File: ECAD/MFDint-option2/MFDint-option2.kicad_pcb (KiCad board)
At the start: 2 copper layers, 113 x 109 mm, 47 parts, among them J1 Conn_02x03_Odd_Even, J2 Conn_01x04, J3 Conn_01x04, J4 Conn_02x03_Odd_Even, J5 Conn_01x04, J6 Conn_01x04, SW11 SW_Push, SW12 SW_Push, SW13 SW_Push, SW14 SW_Push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

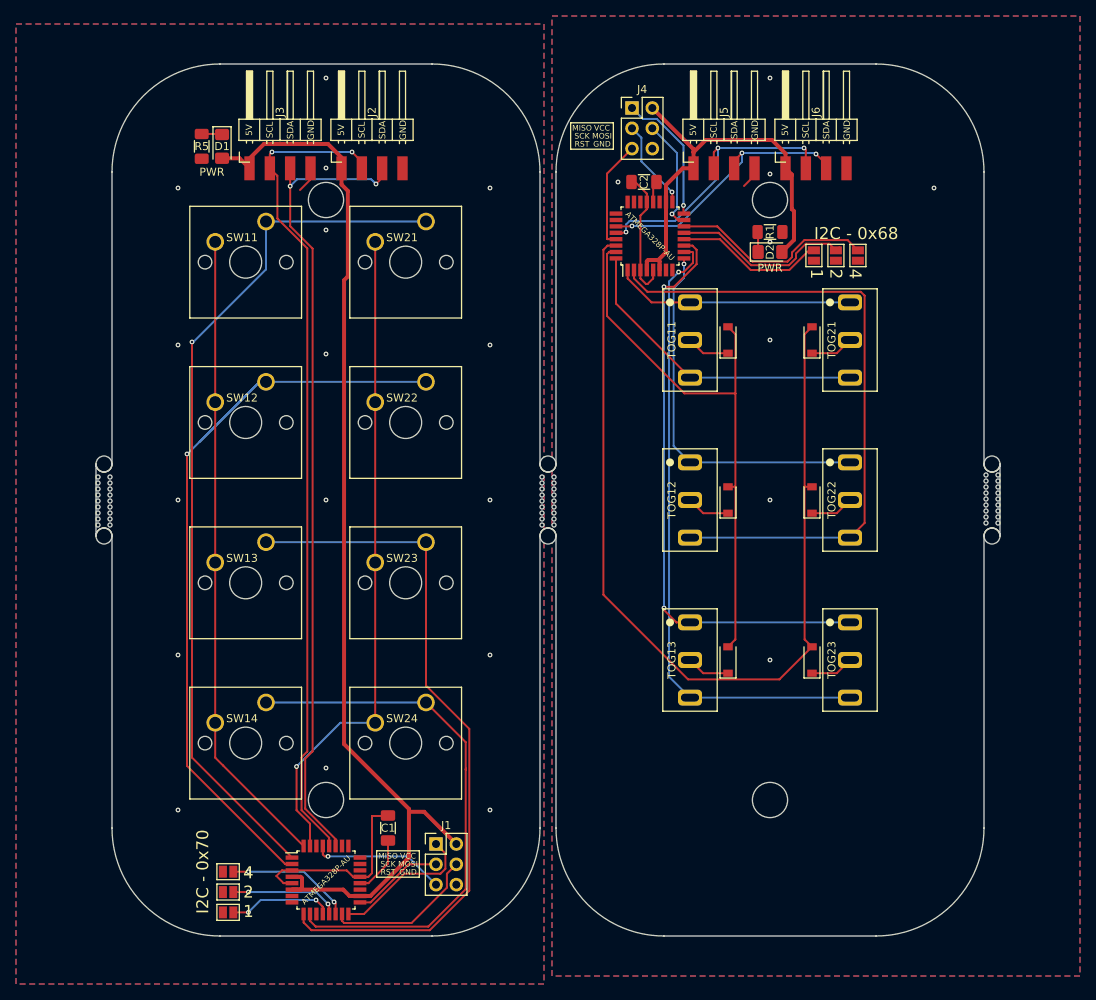
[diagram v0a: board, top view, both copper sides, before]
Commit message: Removing panelisations, adding polyfuses
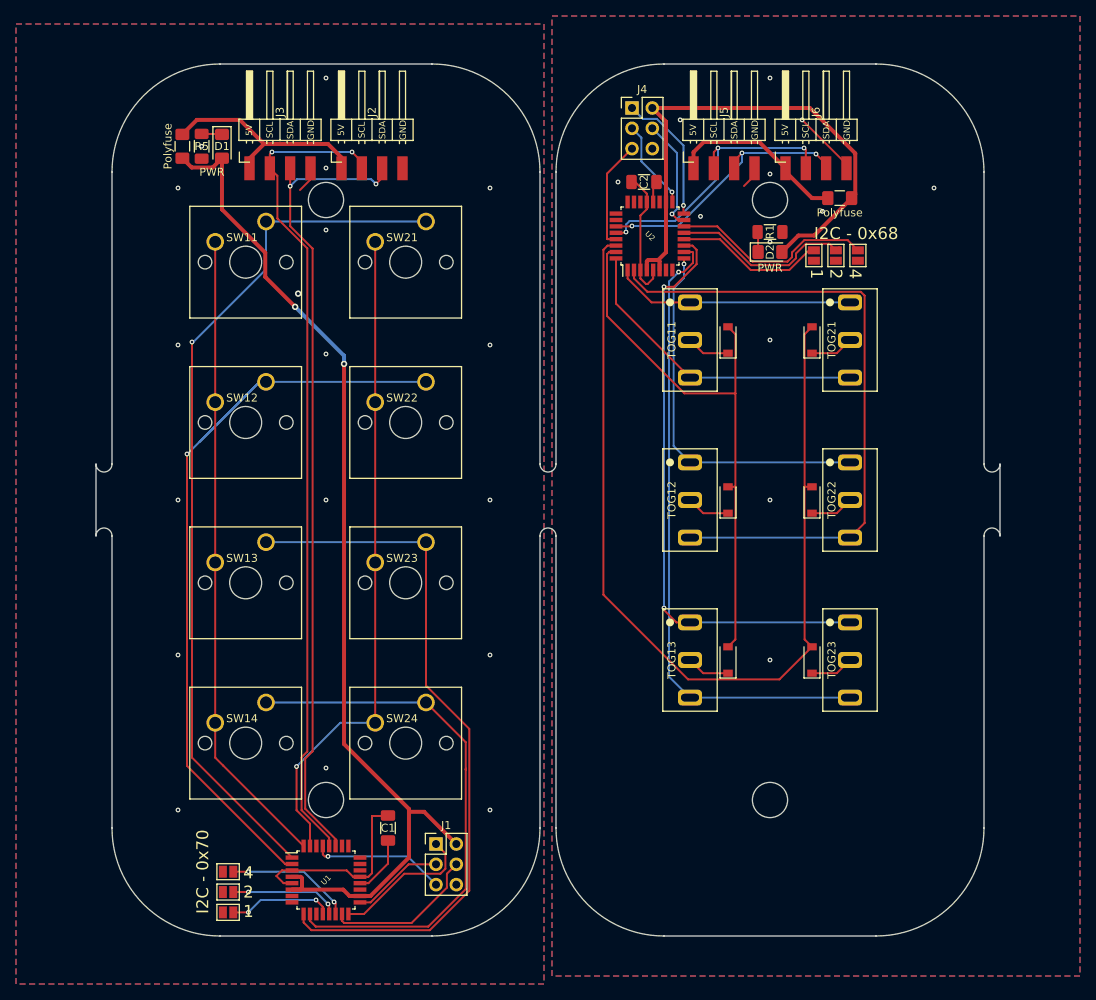
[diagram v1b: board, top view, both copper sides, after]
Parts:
- removed G*** (x2): LOGO, mycustomlibrary:CBB_1inch
- removed REF** (x2): ICSP-Silk, mycustomlibrary:ICSP-Silk
- removed mouse-bite-2mm-slot (x3): VAL**, Panelisation:mouse-bite-2mm-slot-5mm-width
- added Polyfuse: Polyfuse, Fuse:Fuse_1206_3216Metric_Pad1.42x1.75mm_HandSolder, F.Cu at (93.0, 16.8)
- added Polyfuse: Polyfuse, Fuse:Fuse_1206_3216Metric_Pad1.42x1.75mm_HandSolder, F.Cu at (10.8, 10.3)
- renumbered ATMEGA328P-AU to U1, ATMEGA328P-AU to U2
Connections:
- J2 pad 1: +5V -> Net-(F1-Pad2)
- J3 pad 1: +5V -> Net-(F1-Pad2)
- J5 pad 1: VCC -> Net-(F2-Pad2)
- J6 pad 1: VCC -> Net-(F2-Pad2)
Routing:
- net Net-(F1-Pad2): track 0.00 -> 28.6 mm
- net Net-(F2-Pad2): track 0.00 -> 22.5 mm
- net VCC: track 53.9 -> 69.0 mm
- net GNDREF: track 19.4 -> 27.8 mm, vias 8 -> 12
- net +5V: track 138.8 -> 131.4 mm, vias 0 -> 2
- net GND: vias 16 -> 18

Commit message: Change from 1x04 2.54mm headers to 1x05 micro JST
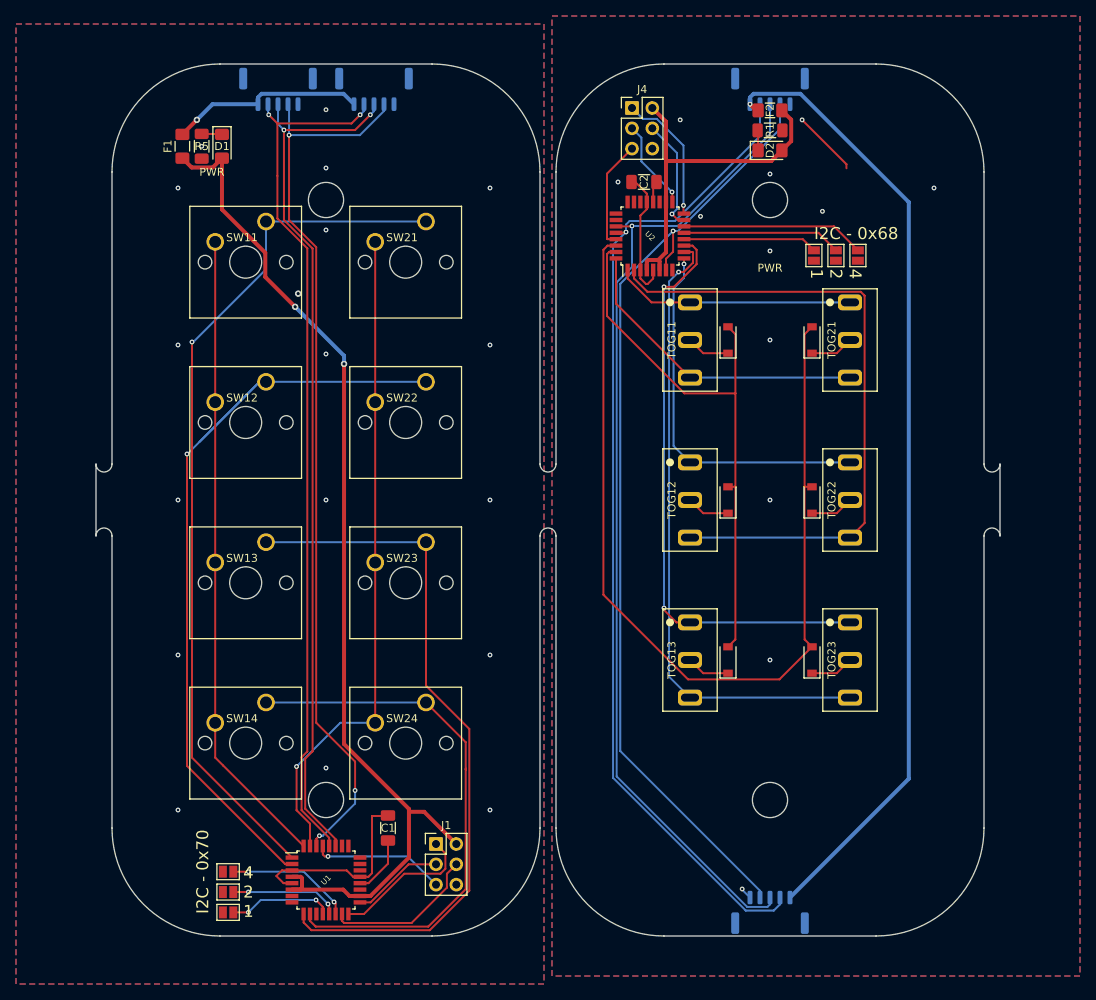
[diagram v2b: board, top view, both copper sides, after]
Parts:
- J2, J3, J5, J6: value Conn_01x04 -> Conn_01x05; footprint mycustomlibrary:PinHeader_1x04_P2.54mm_Horizontal_SMD -> Connector_JST:JST_GH_SM05B-GHS-TB_1x05-1MP_P1.25mm_Horizontal; moved to B.Cu
- moved J5 95.2 mm to (84.2, 106.0), turned to 180 degrees
- moved J2 14.1 mm to (22.8, 3.17), turned to 0 degrees
- moved J3 14.1 mm to (34.8, 3.17), turned to 0 degrees
- moved F2 14.0 mm to (84.2, 5.80)
- moved D2 12.7 mm to (84.2, 10.8)
- moved R1 12.7 mm to (84.2, 8.30)
- moved J6 9.71 mm to (84.2, 3.17), turned to 0 degrees
- renumbered Polyfuse to F1, Polyfuse to F2
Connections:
- J2 pad 4: GND -> /BUS_SIGNAL
- J3 pad 4: GND -> /BUS_SIGNAL
- J5 pad 4: GNDREF -> /BUS_SIGNAL2
- J6 pad 4: GNDREF -> /BUS_SIGNAL2
- U1 pad 30: Net-(U1-Pad30) -> /BUS_SIGNAL
- U2 pad 7: Net-(U2-Pad7) -> /BUS_SIGNAL2
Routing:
- net /BUS_SIGNAL2: track 0.00 -> 120.3 mm, vias 0 -> 1
- net /BUS_SIGNAL: track 0.00 -> 112.4 mm, vias 0 -> 3
- net Net-(F2-Pad2): track 22.5 -> 120.9 mm, vias 0 -> 1
- net SDA2: track 34.1 -> 124.3 mm, vias 3 -> 1
- net SCL2: track 36.0 -> 125.3 mm, vias 3 -> 1
- net VCC: track 69.0 -> 45.1 mm
- net SDA: track 101.5 -> 110.1 mm
- net SCL: track 103.1 -> 108.8 mm
- net Net-(F1-Pad2): track 28.6 -> 24.6 mm, vias 0 -> 1
- net GND: track 27.5 -> 24.3 mm
- net /4line2: track 25.5 -> 23.0 mm
- net /2line2: track 23.0 -> 20.5 mm
- net /1line2: track 18.9 -> 16.8 mm
- net GNDREF: track 27.8 -> 26.5 mm
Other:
- board text removed: "5V SCL SDA GND"

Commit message: Swap bus connector to 4-pin JST-GH
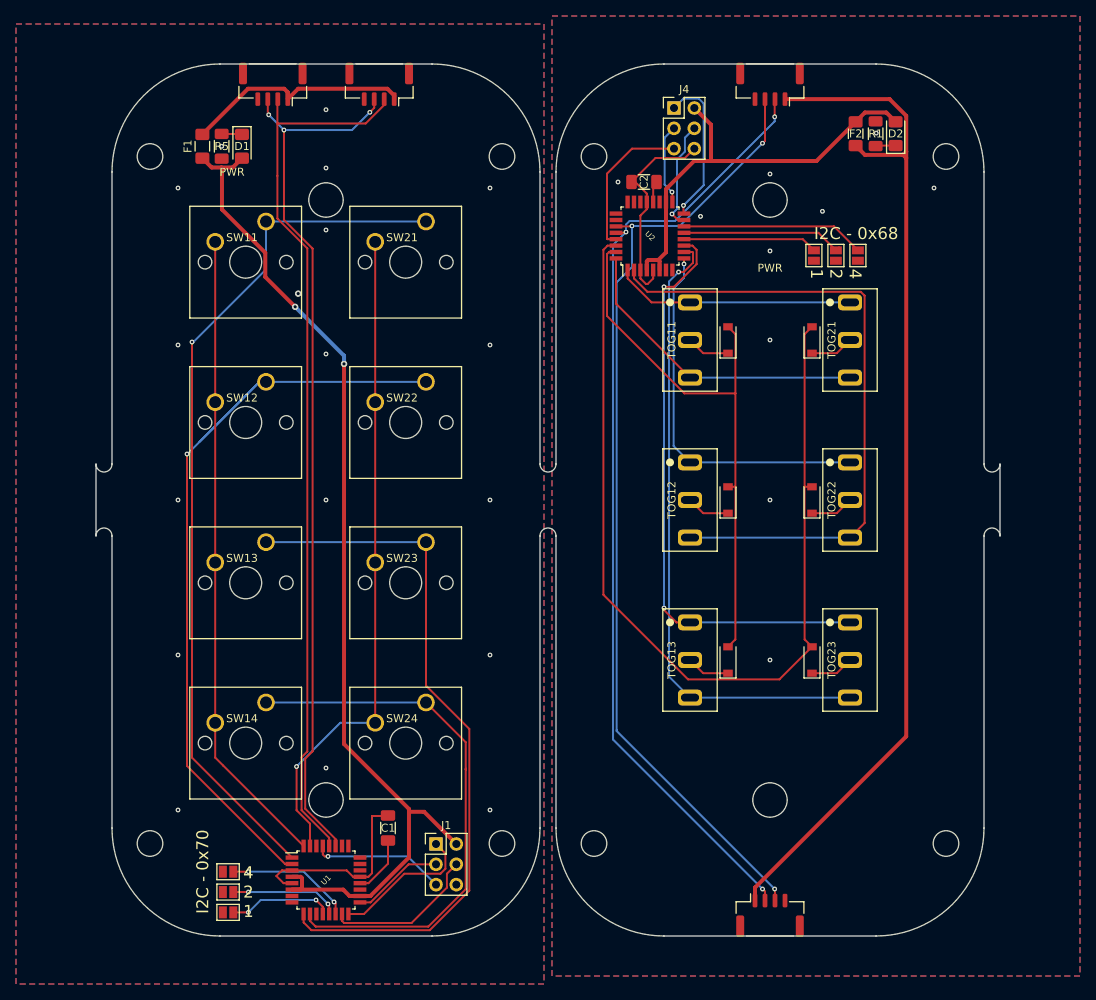
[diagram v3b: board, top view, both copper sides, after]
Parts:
- added H1: MountingHole, MountingHole:MountingHole_4.3mm_M4, F.Cu at (28.8, 17.0)
- added H10: MountingHole, MountingHole:MountingHole_3.2mm_M3, F.Cu at (106.2, 11.6)
- added H11: MountingHole, MountingHole:MountingHole_3.2mm_M3, F.Cu at (62.2, 97.4)
- added H12: MountingHole, MountingHole:MountingHole_3.2mm_M3, F.Cu at (106.2, 97.4)
- added H2: MountingHole, MountingHole:MountingHole_4.3mm_M4, F.Cu at (28.8, 92.0)
- added H3: MountingHole, MountingHole:MountingHole_4.3mm_M4, F.Cu at (84.2, 17.0)
- added H4: MountingHole, MountingHole:MountingHole_4.3mm_M4, F.Cu at (84.2, 92.0)
- added H5: MountingHole, MountingHole:MountingHole_3.2mm_M3, F.Cu at (50.8, 11.6)
- added H6: MountingHole, MountingHole:MountingHole_3.2mm_M3, F.Cu at (6.75, 11.6)
- added H7: MountingHole, MountingHole:MountingHole_3.2mm_M3, F.Cu at (6.75, 97.4)
- added H8: MountingHole, MountingHole:MountingHole_3.2mm_M3, F.Cu at (50.8, 97.4)
- added H9: MountingHole, MountingHole:MountingHole_3.2mm_M3, F.Cu at (62.2, 11.6)
- J2, J3, J5, J6: value Conn_01x05 -> Conn_01x04; footprint Connector_JST:JST_GH_SM05B-GHS-TB_1x05-1MP_P1.25mm_Horizontal -> Connector_JST:JST_GH_SM04B-GHS-TB_1x04-1MP_P1.25mm_Horizontal; moved to F.Cu
- moved J5 103.5 mm to (84.2, 2.54)
- moved J6 103.3 mm to (84.2, 106.4)
- moved D2 15.8 mm to (100.0, 8.71), turned to 90 degrees
- moved R1 13.2 mm to (97.5, 8.71), turned to 90 degrees
- moved F2 11.1 mm to (95.0, 8.71), turned to 270 degrees
- moved J4 5.25 mm to (72.2, 5.50)
- moved D1 2.50 mm to (18.2, 10.3)
- moved F1 2.50 mm to (13.3, 10.3)
- moved R5 2.50 mm to (15.7, 10.3)
- moved J2 0.91 mm to (22.1, 2.54), turned to 180 degrees
- moved J3 0.91 mm to (35.4, 2.54), turned to 180 degrees
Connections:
- J2 pad 4: /BUS_SIGNAL -> GND
- J3 pad 4: /BUS_SIGNAL -> GND
- J5 pad 4: /BUS_SIGNAL2 -> GNDREF
- J6 pad 4: /BUS_SIGNAL2 -> GNDREF
- U1 pad 30: /BUS_SIGNAL -> Net-(U1-Pad30)
- U2 pad 7: /BUS_SIGNAL2 -> Net-(U2-Pad7)
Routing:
- net /BUS_SIGNAL2: track 120.3 -> 0.00 mm, vias 1 -> 0
- net /BUS_SIGNAL: track 112.4 -> 0.00 mm, vias 3 -> 0
- net VCC: track 45.1 -> 53.8 mm
- net Net-(F2-Pad2): track 120.9 -> 129.5 mm, vias 1 -> 0
- net RESET2: track 13.7 -> 18.9 mm
- net SCL2: track 125.3 -> 121.1 mm, vias 1 -> 3
- net Net-(F1-Pad2): track 24.6 -> 28.7 mm, vias 1 -> 0
- net SCL: track 108.8 -> 111.7 mm, vias 2 -> 0
- net SDA2: track 124.3 -> 121.6 mm, vias 1 -> 3
- net MISO2: track 16.9 -> 19.3 mm
- net SCK2: track 11.3 -> 10.1 mm
- net +5V: track 131.4 -> 130.3 mm
- net SDA: track 110.1 -> 111.2 mm, vias 2 -> 3
- net GNDREF: track 26.5 -> 26.3 mm, vias 12 -> 10
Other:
- outline, holes or cut-outs redrawn
